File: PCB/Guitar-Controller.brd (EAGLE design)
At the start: 160 x 100 mm, 33 parts

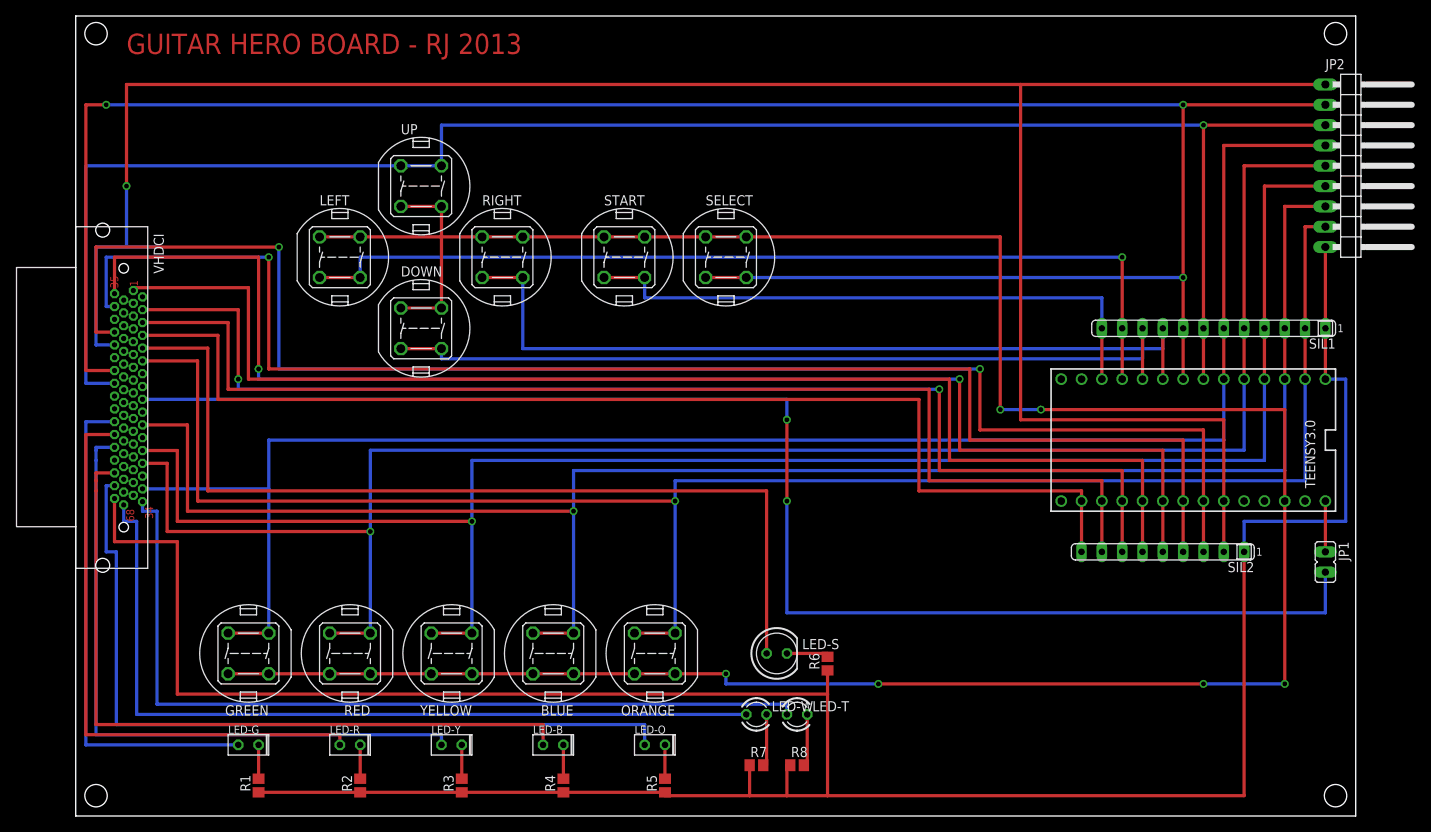
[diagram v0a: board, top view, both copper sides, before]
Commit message: PCB: Changed all pin connections to use bottom layer
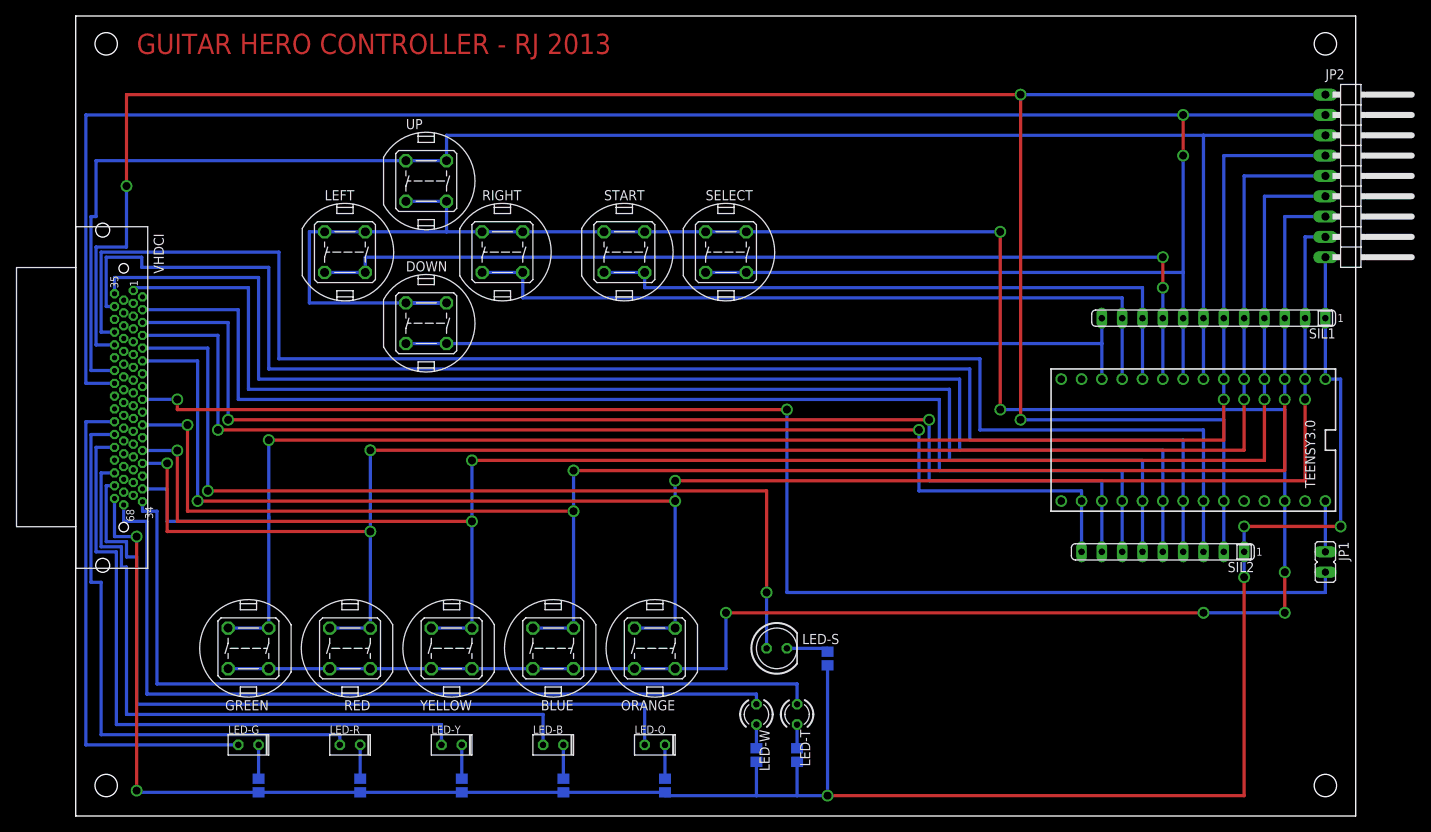
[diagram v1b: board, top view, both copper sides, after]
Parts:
- moved R7 1.27 mm to (85.1, 7.62), flipped to the bottom, turned to 90 degrees
- moved R8 1.27 mm to (90.2, 7.62), flipped to the bottom, turned to 90 degrees
- moved JP2 1.27 mm to (160.0, 80.0)
- moved SIL1 1.27 mm to (142.2, 62.2)
- moved LEFT 0.90 mm to (33.7, 70.5)
- moved UP 0.90 mm to (43.8, 79.4)
- moved DOWN 0.90 mm to (43.8, 61.6)
- moved RIGHT 0.64 mm to (53.3, 70.5)
- moved SELECT 0.64 mm to (81.3, 70.5)
- moved START 0.64 mm to (68.6, 70.5)
- moved BLUE 0.63 mm to (59.7, 21.0)
- moved GREEN 0.63 mm to (21.6, 21.0)
- moved LED-S 0.63 mm to (87.6, 21.0)
- moved ORANGE 0.63 mm to (72.4, 21.0)
- moved R6 0.63 mm to (94.0, 19.7), flipped to the bottom
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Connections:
- net DOWN: now also SIL1.12, TEENSY3.0.10; no longer SIL1.10, TEENSY3.0.8
- net GND: no longer VHDCI.P$2
- net LEFT: now also SIL1.9, TEENSY3.0.7; no longer SIL1.11, TEENSY3.0.9
- net RIGHT: now also SIL1.11, TEENSY3.0.9; no longer SIL1.9, TEENSY3.0.7
- net SELECT: now also VHDCI.P$49; no longer VHDCI.P$47
- net START: now also SIL1.10, TEENSY3.0.8; no longer SIL1.12, TEENSY3.0.10
- net UP: now also VHDCI.P$47; no longer VHDCI.P$49
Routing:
- net GND: track 344.7 -> 284.4 mm, vias 0 -> 6
- net 3V3: track 332.7 -> 348.6 mm
- net RIGHT: track 102.9 -> 93.3 mm
- net DOWN: track 104.1 -> 94.6 mm
- net WHAMMY7: track 276.2 -> 269.8 mm, vias 1 -> 3
- net START: track 74.9 -> 80.6 mm
- net UP: track 222.5 -> 217.1 mm, vias 1 -> 0
- net 5V: track 179.6 -> 174.5 mm
- net WHAMMY4: track 171.2 -> 166.1 mm, vias 2 -> 0
- net N$40: track 6.77 -> 2.96 mm
- net LEFT: track 118.1 -> 121.9 mm, vias 1 -> 2
- net N$39: track 6.35 -> 2.96 mm
- net GREEN: track 213.9 -> 216.7 mm, vias 0 -> 2
- net WHAMMY6: track 189.5 -> 186.9 mm, vias 2 -> 0
- net YELLOW: track 217.7 -> 215.8 mm, vias 1 -> 4
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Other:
- board text added: "GUITAR HERO CONTROLLER - RJ 2013"
- board text removed: "GUITAR HERO BOARD - RJ 2013"

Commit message: PCB: Final PCB changes (hopefully)
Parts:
- moved JP2 32.0 mm to (128.3, 76.2)
- moved SIL1 31.8 mm to (110.5, 61.6)
- moved JP1 31.8 mm to (124.5, 31.8)
- moved SIL2 31.7 mm to (104.1, 33.0)
- moved TEENSY3.0 31.7 mm to (108.0, 47.0)
- moved LED-S 11.9 mm to (82.5, 31.8)
- moved R6 11.9 mm to (88.9, 30.5)
- moved ORANGE 11.4 mm to (68.6, 31.8)
- moved YELLOW 11.4 mm to (43.2, 31.8)
- moved BLUE 11.4 mm to (55.9, 31.8)
- moved GREEN 11.4 mm to (17.8, 31.8)
- moved R2 11.4 mm to (31.8, 14.6)
- moved R4 11.4 mm to (57.1, 14.6)
- moved R5 11.4 mm to (69.8, 14.6)
- moved RED 11.4 mm to (30.5, 31.8)
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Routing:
- net SELECT: track 284.8 -> 216.2 mm
- net GND: track 284.4 -> 226.0 mm, vias 6 -> 4
- net GREEN: track 216.7 -> 165.6 mm
- net RED: track 218.0 -> 167.8 mm
- net YELLOW: track 215.8 -> 166.9 mm
- net BLUE: track 215.2 -> 167.5 mm
- net ORANGE: track 219.4 -> 173.0 mm
- net WHAMMY7: track 269.8 -> 228.5 mm
- net 3V3: track 348.6 -> 308.6 mm, vias 6 -> 4
- net UP: track 217.1 -> 179.0 mm
- net WHAMMY6: track 186.9 -> 155.2 mm
- net WHAMMY5: track 178.7 -> 146.9 mm
- net WHAMMY4: track 166.1 -> 134.3 mm
- net WHAMMY2: track 152.7 -> 121.0 mm
- net WHAMMY1: track 148.6 -> 116.8 mm
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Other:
- board size 160 x 100 mm -> 128.2 x 87 mm
- board text added: "Aux Out"
- board text added: "BLUE"
- board text added: "D-PAD"
- board text added: "GREEN"
- board text added: "Guitar Hero Controller / RJ 2013"
- board text added: "ORANGE"
- board text added: "POW"
- board text added: "RED"
- board text added: "SELECT"
- board text added: "START"
- board text added: "STRUM"
- board text added: "TLT"
- board text added: "Teensy 3.0"
- board text added: "VHDCI In"
- board text added: "WMY"
- board text added: "YELLOW"
- board text removed: "GUITAR HERO CONTROLLER - RJ 2013"

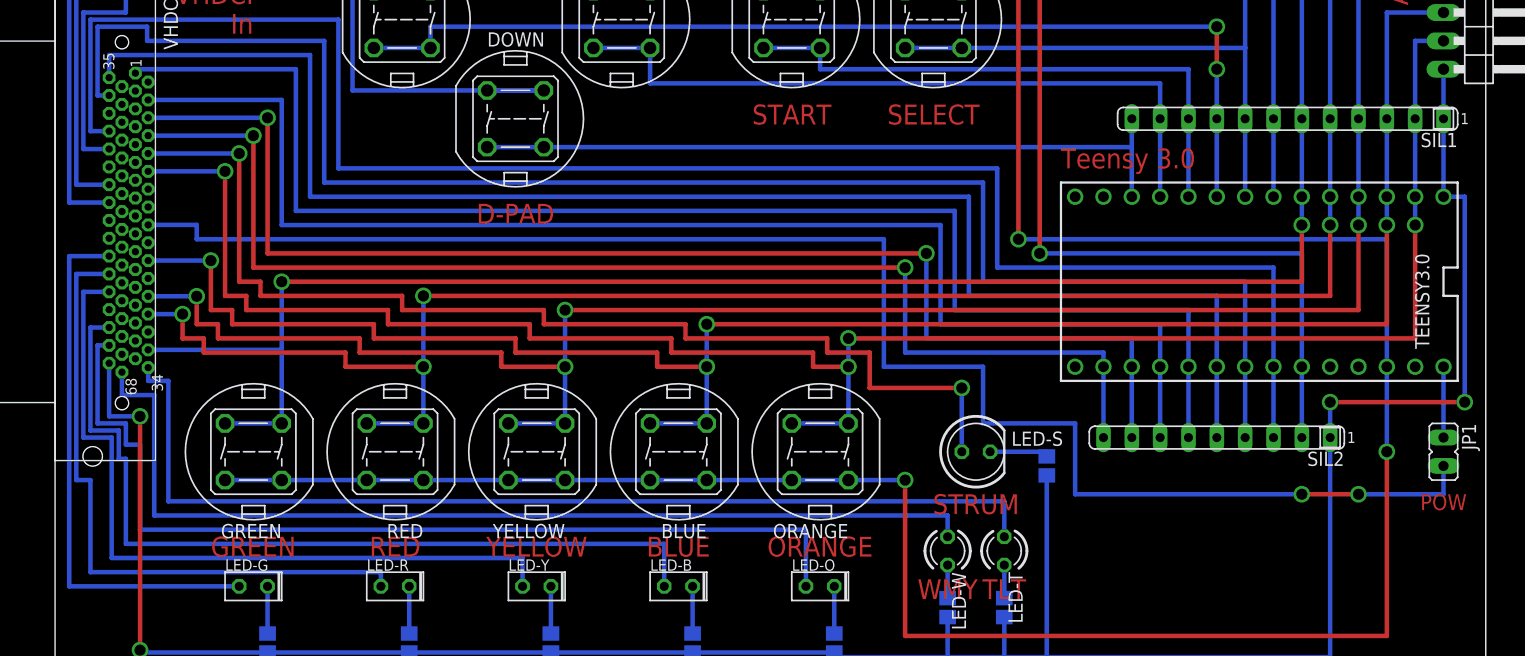
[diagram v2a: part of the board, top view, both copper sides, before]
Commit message: PCB: Fixed errors on VHDC connector and changed SILs SIL change is to work with what is available in department
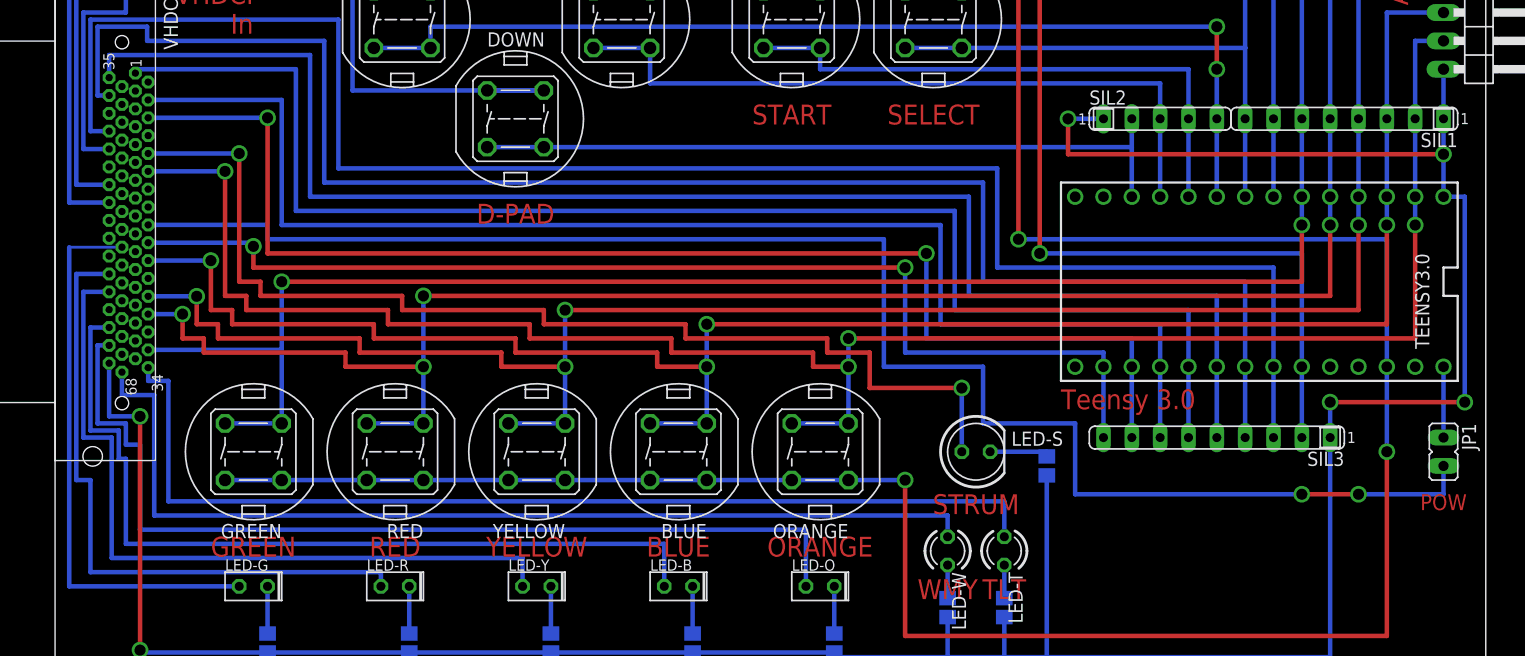
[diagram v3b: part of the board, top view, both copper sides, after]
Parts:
- added SIL3: 1k, resistor-sil:SIL9
- SIL1: device resistor-sil:SIL12 -> resistor-sil:SIL8
- SIL2: device resistor-sil:SIL9 -> resistor-sil:SIL5
- moved SIL2 29.0 mm to (99.1, 61.6), turned to 0 degrees
- moved SIL1 5.08 mm to (115.6, 61.6)
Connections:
- net DOWN: now also SIL2.2; no longer SIL1.12
- net GND: now also SIL3.1
- net LEDG: now also VHDCI.P$54; no longer VHDCI.P$55
- net LEFT: now also SIL2.5; no longer SIL1.9
- net RIGHT: now also SIL2.3; no longer SIL1.11
- net START: now also SIL2.4; no longer SIL1.10
- net WHAMMY0: now also SIL3.9, VHDCI.P$20; no longer SIL2.9, VHDCI.P$8
- net WHAMMY1: now also SIL3.8; no longer SIL2.8
- net WHAMMY2: now also SIL3.7; no longer SIL2.7
- net WHAMMY3: now also SIL3.6; no longer SIL2.6
- net WHAMMY4: now also SIL3.5; no longer SIL2.5
- net WHAMMY5: now also SIL3.4; no longer SIL2.4
- net WHAMMY6: now also SIL3.3; no longer SIL2.3
- net WHAMMY7: now also SIL3.2; no longer SIL2.2
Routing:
- net GND: track 226.0 -> 266.0 mm, vias 4 -> 6
- net WHAMMY0: track 112.7 -> 103.1 mm
- net LEDG: track 48.4 -> 50.4 mm
